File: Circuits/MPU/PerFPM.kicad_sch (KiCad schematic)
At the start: 46 parts, among them Q1 SI4421DY, Q2 MMBTA92, Q3 MMBTA92, U3 LT1715, U4 ADA4805-2ARMZ, U5 ADA4805-2ARMZ, U6 ADA4805-2ARMZ

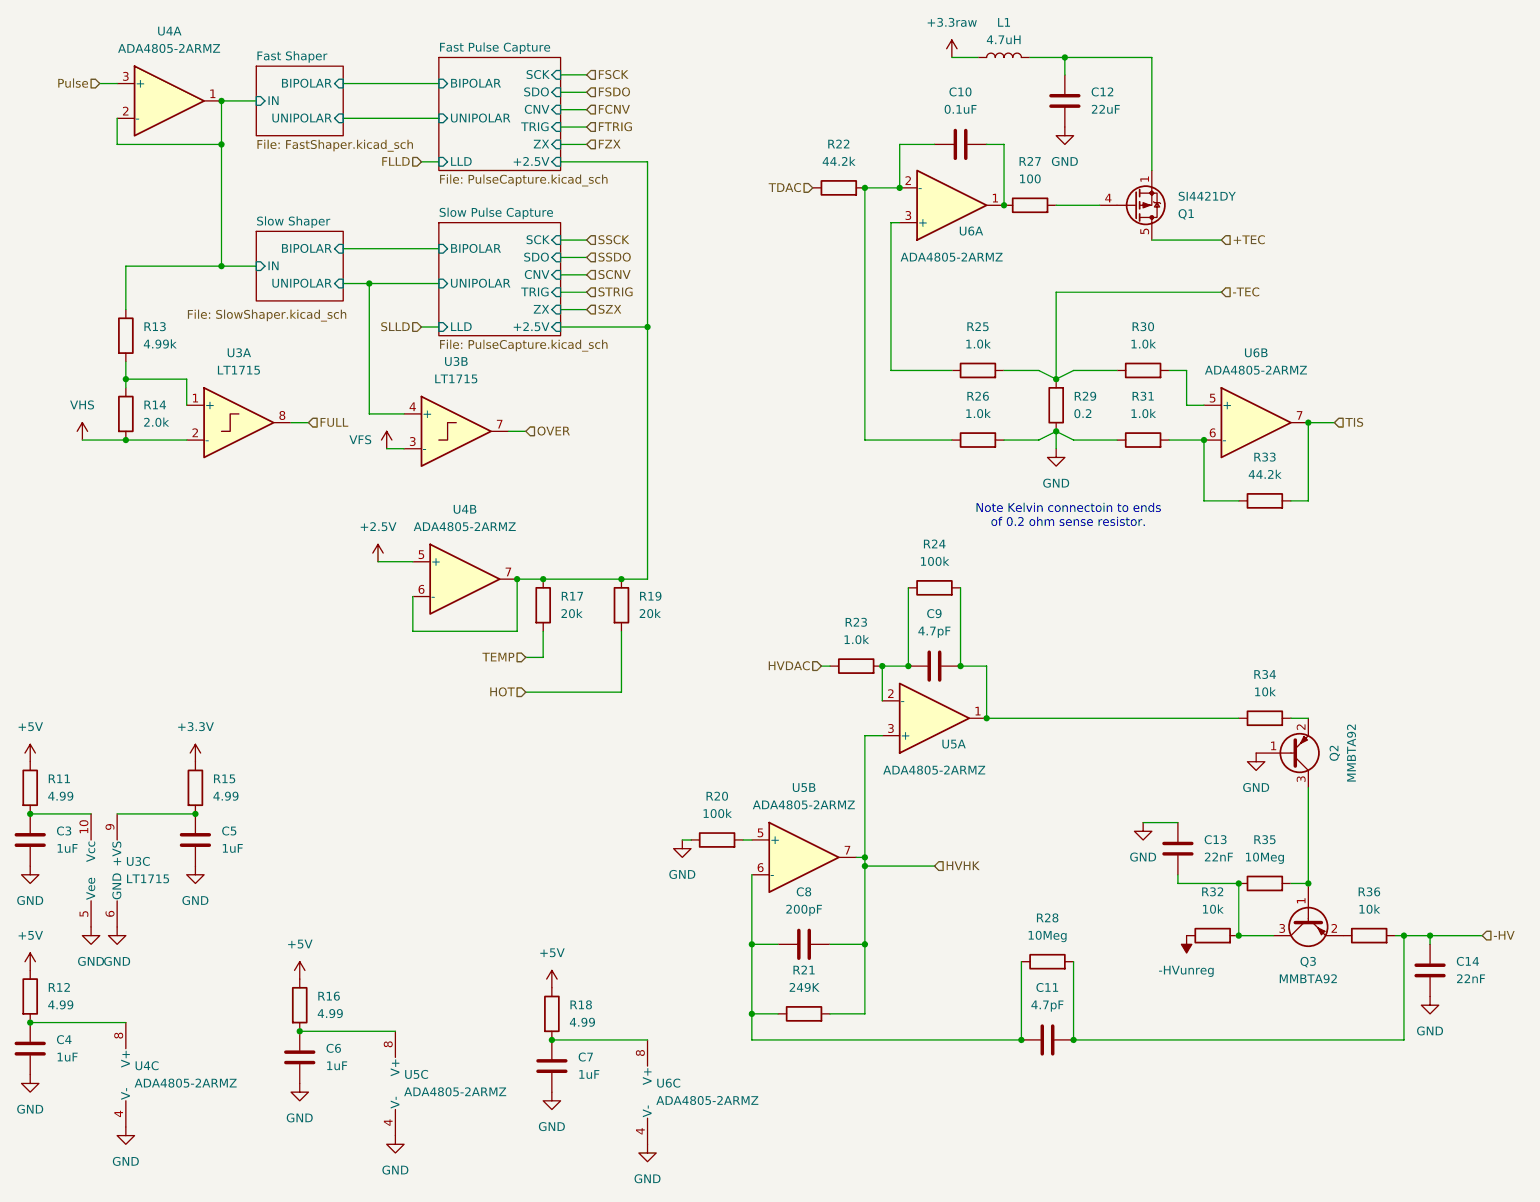
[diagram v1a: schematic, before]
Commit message: PPS is RS422, add MXINH
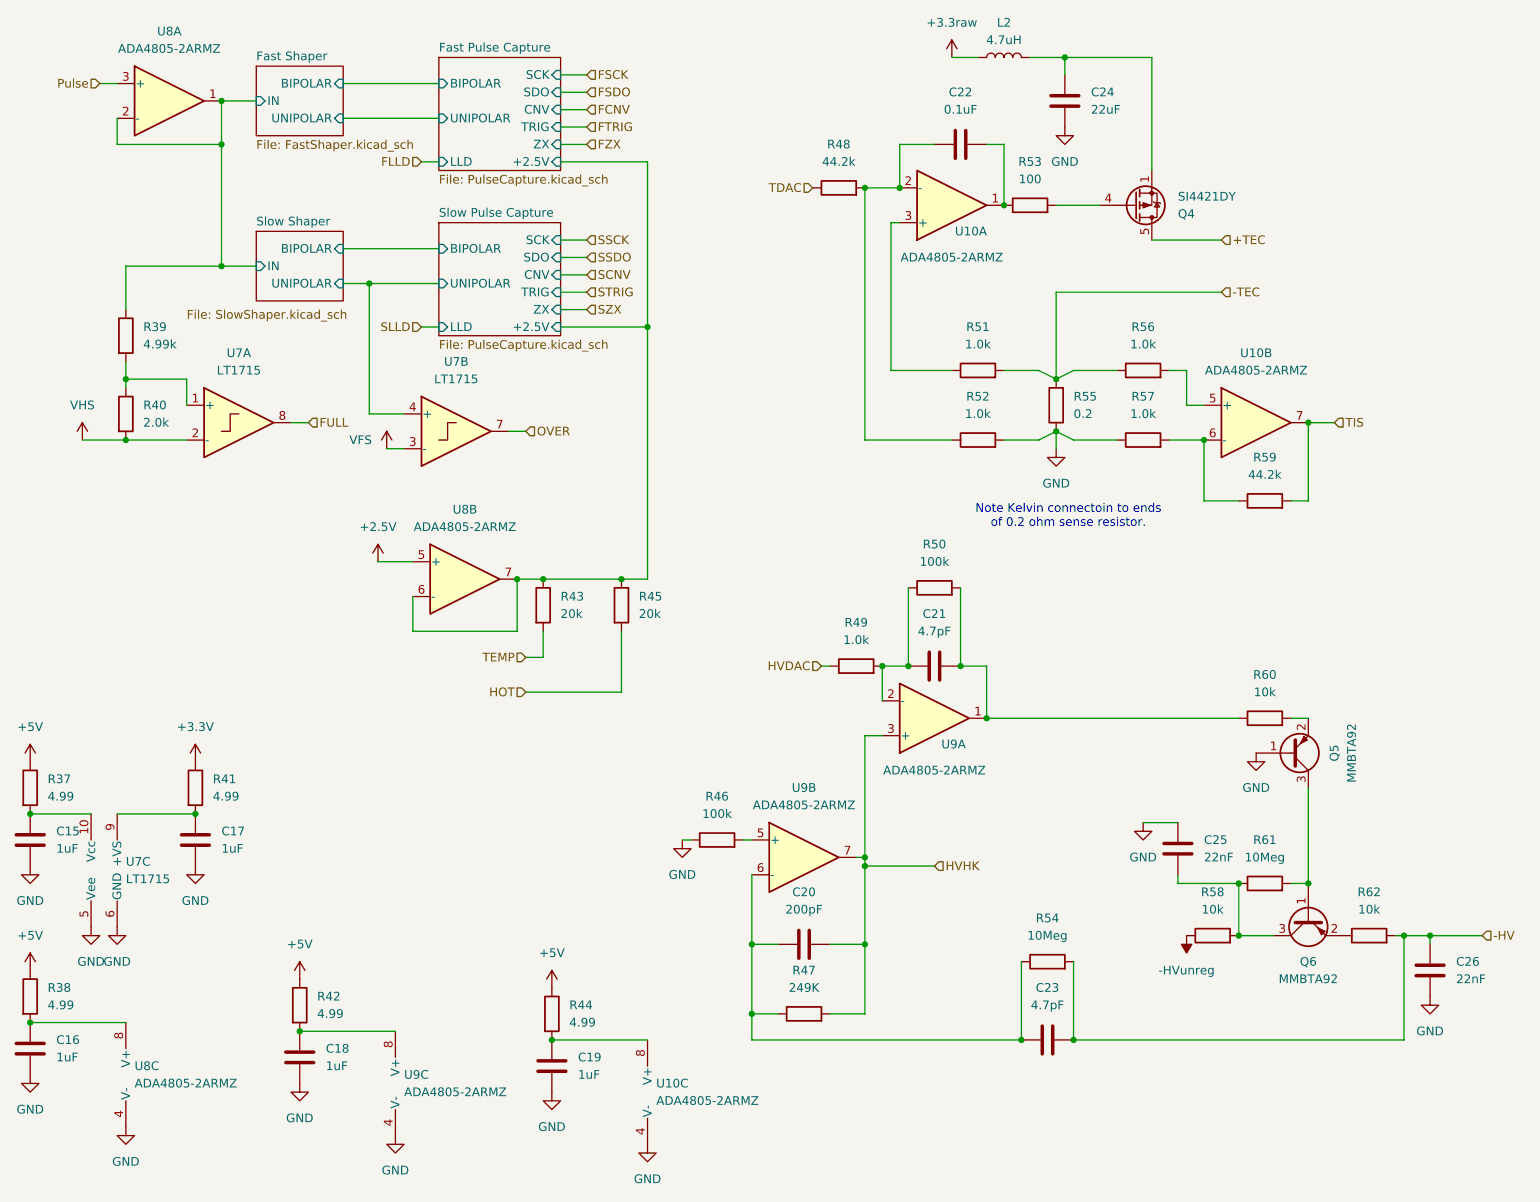
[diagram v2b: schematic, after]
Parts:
- renumbered C3 to C15, C4 to C16, C5 to C17, C6 to C18, C7 to C19, C8 to C20, C9 to C21, C10 to C22, C11 to C23, C12 to C24, C13 to C25, C14 to C26, L1 to L2, Q1 to Q4, Q2 to Q5, Q3 to Q6, R11 to R37, R12 to R38, R13 to R39, R14 to R40, R15 to R41, R16 to R42, R17 to R43, R18 to R44, R19 to R45, R20 to R46, R21 to R47, R22 to R48, R23 to R49, R24 to R50, R25 to R51, R26 to R52, R27 to R53, R28 to R54, R29 to R55, R30 to R56, R31 to R57, R32 to R58, R33 to R59, R34 to R60, R35 to R61, R36 to R62, U6 to U10, U3 to U7, U4 to U8, U5 to U9

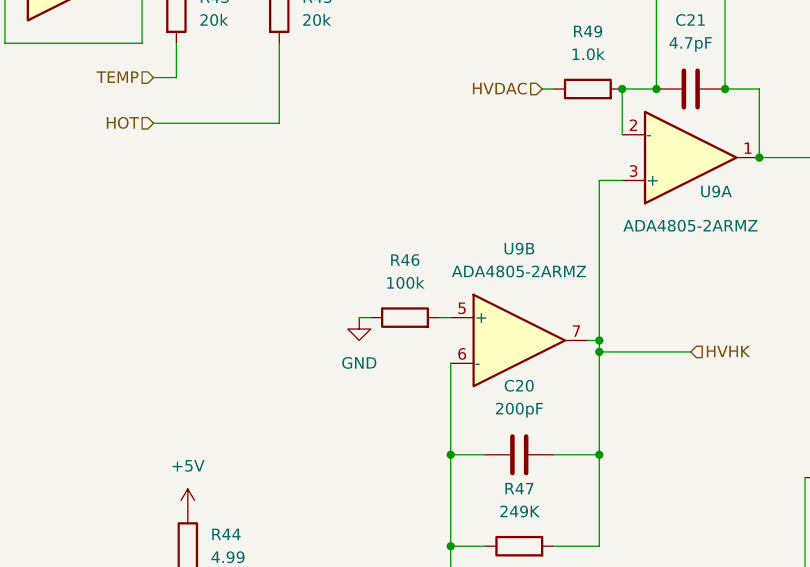
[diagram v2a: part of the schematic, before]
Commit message: Fix errors found by Norm Dobson
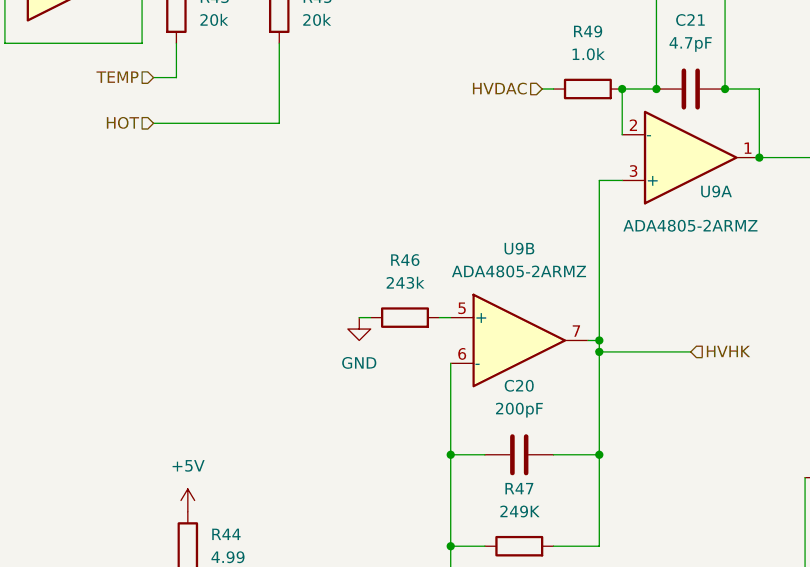
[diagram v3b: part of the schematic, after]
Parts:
- R46: value 100k -> 243k
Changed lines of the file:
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@@
 			)
 		)
-		(property "Value" "100k"
+		(property "Value" "243k"
 			(at 135.89 134.62 90)
 			(effects
